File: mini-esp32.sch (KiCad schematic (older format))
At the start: 46 parts, among them J1 BAT, J2 USB_B_Micro, J5 Conn_01x18, J6 Conn_01x18, Q1 AO3401A, Q2 S8050, Q3 S8050, Q4 2N7002, SW1 RESET, U1 ESP32-WROOM-32D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

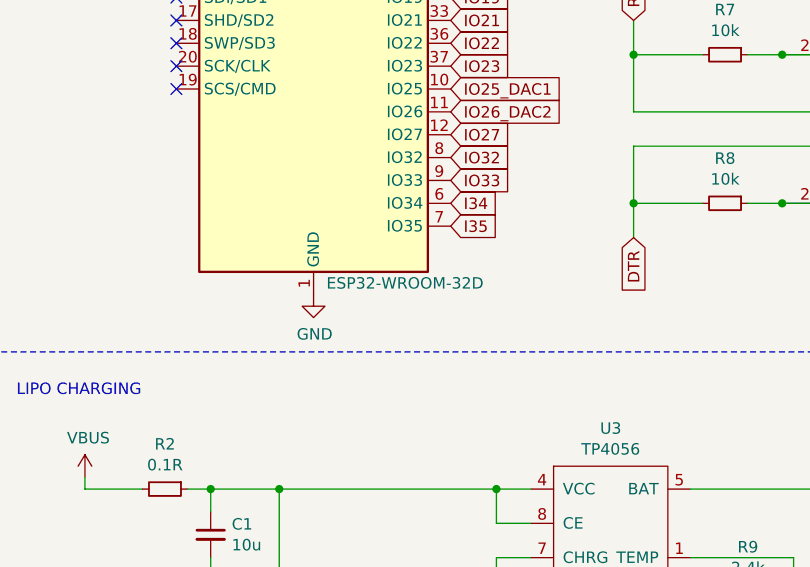
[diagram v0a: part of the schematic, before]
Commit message: Fix USB Micro B footprint to official one
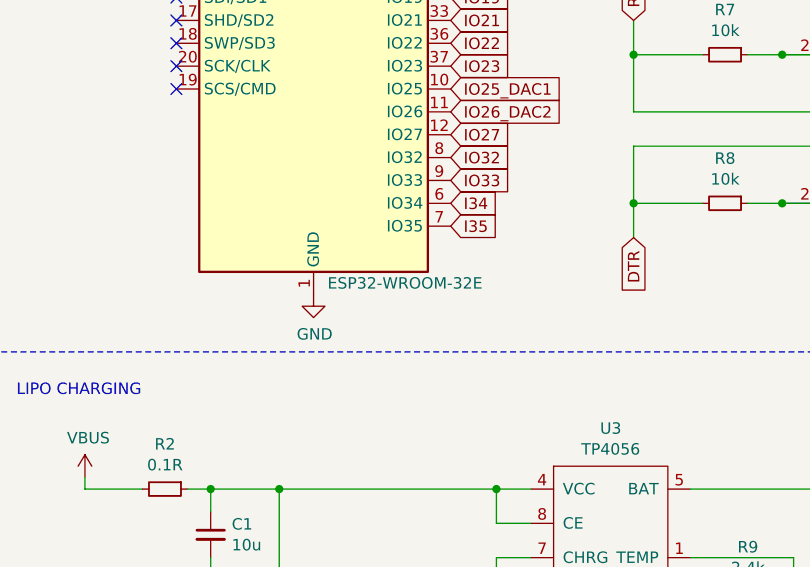
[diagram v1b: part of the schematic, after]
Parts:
- J2: footprint serialx:C10418 -> LCSC:USB_Micro-B_Jing-C10418-A01SB141B1-067
- U1: value ESP32-WROOM-32D -> ESP32-WROOM-32E; LCSC Part # (none) -> C701343
- U2: LCSC Part # (none) -> C841192
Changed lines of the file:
@@
 P 1950 4350
 F 0 "U1" H 2400 5700 50  0000 C CNN
-F 1 "ESP32-WROOM-32D" H 2350 3000 50  0000 C CNN
+F 1 "ESP32-WROOM-32E" H 2350 3000 50  0000 C CNN
 F 2 "RF_Module:ESP32-WROOM-32" H 1950 2850 50  0001 C CNN
 F 3 "https://www.espressif.com/sites/default/files/documentation/esp32-wroom-32d_esp32-wroom-32u_datasheet_en.pdf" H 1650 4400 50  0001 C CNN
+F 4 "C701343" H 1950 4350 50  0001 C CNN "LCSC Part #"
 	1    1950 4350
 	1    0    0    -1
@@
 F 2 "Package_TO_SOT_SMD:TSOT-23-5" H 3200 1150 50  0001 C CNN
 F 3 "" H 3200 1150 50  0001 C CNN
+F 4 "C841192" H 3200 1150 50  0001 C CNN "LCSC Part #"
 	1    3200 1150
 	1    0    0    -1
@@
 F 0 "J2" H 5657 4017 50  0000 C CNN
 F 1 "USB_B_Micro" H 5657 3926 50  0000 C CNN
-F 2 "serialx:C10418" H 5750 3500 50  0001 C CNN
+F 2 "LCSC:USB_Micro-B_Jing-C10418-A01SB141B1-067" H 5750 3500 50  0001 C CNN
 F 3 "~" H 5750 3500 50  0001 C CNN
 F 4 "C10418" H 5600 3550 50  0001 C CNN "LCSC Part #"

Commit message: Improved routing. Internal layers are not used anymore for routing.
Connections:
- net VBUS: no longer Q1.1 (G)
- net at D1.2 (A), FB1.1: now also Q1.1 (G)
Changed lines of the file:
@@
 $EndComp
-Wire Wire Line
-	1100 1000 1100 1100
 Wire Wire Line
 	1100 1500 1200 1500
@@
 	1100 1500 1100 1750
 Wire Wire Line
-	1500 1100 1100 1100
-Connection ~ 1100 1100
-Wire Wire Line
-	1100 1100 1100 1500
+	1500 1100 1450 1100
 $Comp
 L power:GND #PWR0114
@@
 NoConn ~ 10150 4150
 NoConn ~ 10150 4400
+Wire Wire Line
+	1450 1100 1450 1500
+Connection ~ 1450 1500
+Wire Wire Line
+	1100 1000 1100 1500
 $EndSCHEMATC

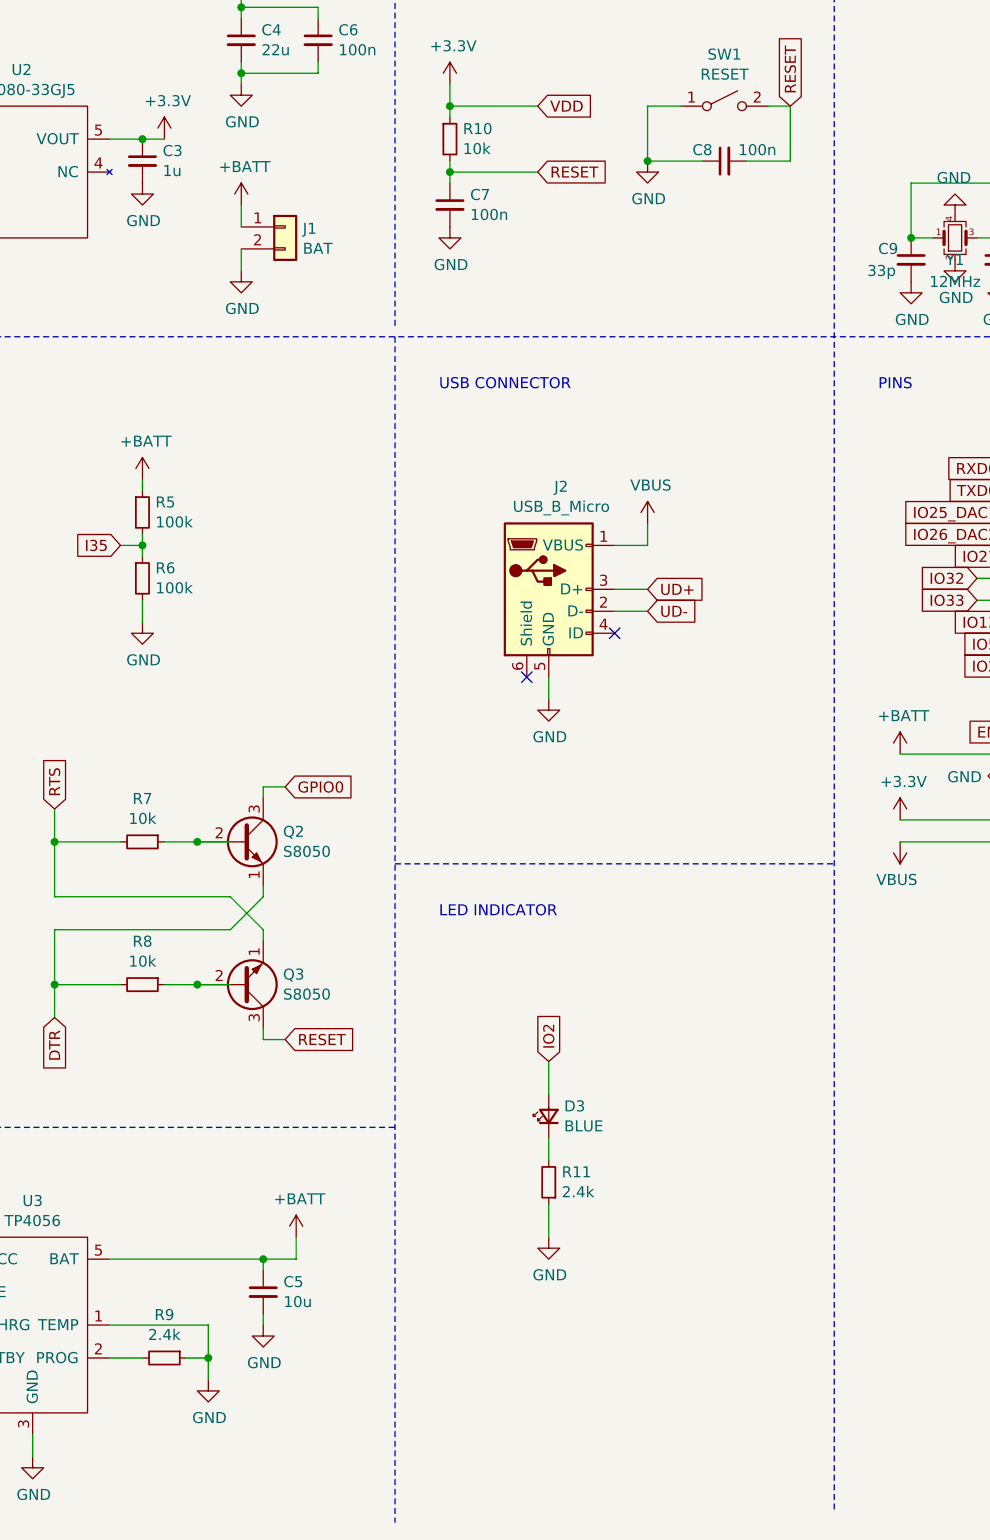
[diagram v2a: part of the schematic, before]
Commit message: Add FS312F-G battery protection IC
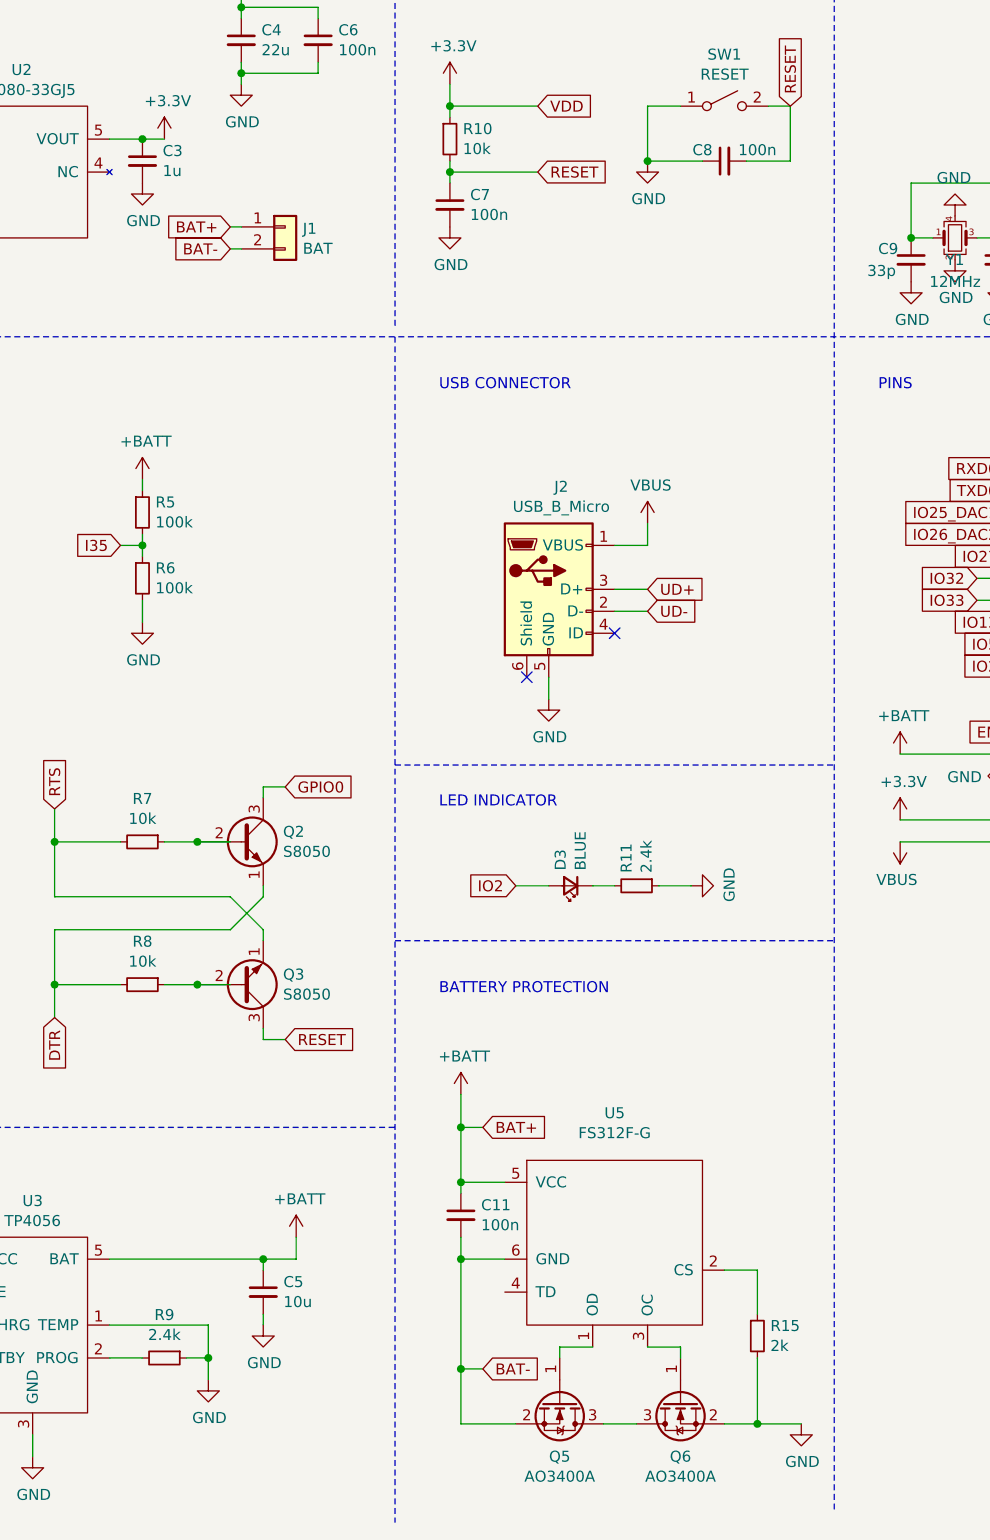
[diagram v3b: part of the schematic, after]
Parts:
- added C11: 100n, Capacitor_SMD:C_0402_1005Metric, symbol Device:C_Small
- added Q5, Q6: AO3400A, Package_TO_SOT_SMD:SOT-23, symbol Transistor_FET:AO3400A
- added R15: 2k, Resistor_SMD:R_0402_1005Metric, symbol Device:R_Small
- added U5: FS312F-G, Package_TO_SOT_SMD:SOT-23-6, symbol myLib:FS312F-G
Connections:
- net +BATT: now also C11.1, U5.5 (VCC)
- net GND: now also Q6.2 (S), R15.2; no longer J1.2 (Pin_2)
- new net: Q5.1 (G), U5.1 (OD)
- new net: R15.1, U5.2 (CS)
- new net: Q6.1 (G), U5.3 (OC)
- new net: Q5.3 (D), Q6.3 (D)
- new net BAT-: C11.2, J1.2 (Pin_2), Q5.2 (S), U5.6 (GND)
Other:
- note added: "BATTERY PROTECTION"
- moved on the sheet: D3, R11
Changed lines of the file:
@@
 $EndComp
-$Comp
-L power:GND #PWR0116
-U 1 1 5F8AD9AA
-P 4200 2100
-F 0 "#PWR0116" H 4200 1850 50  0001 C CNN
-F 1 "GND" H 4205 1927 50  0000 C CNN
-F 2 "" H 4200 2100 50  0001 C CNN
-F 3 "" H 4200 2100 50  0001 C CNN
-	1    4200 2100
-	1    0    0    -1
-$EndComp
-$Comp
-L power:+BATT #PWR0117
-U 1 1 5F8ADEC7
-P 4200 1800
-F 0 "#PWR0117" H 4200 1650 50  0001 C CNN
-F 1 "+BATT" H 4215 1973 50  0000 C CNN
-F 2 "" H 4200 1800 50  0001 C CNN
-F 3 "" H 4200 1800 50  0001 C CNN
-	1    4200 1800
-	1    0    0    -1
-$EndComp
-Wire Wire Line
-	4200 1900 4200 1800
-Wire Wire Line
-	4200 2000 4200 2100
 $Comp
 L power:GND #PWR0118
@@
 Wire Notes Line
 	4900 2400 4900 7800
-Text GLabel 5600 5700 1    50   Input ~ 0
-IO2
-$Comp
-L Device:LED_Small D3
-U 1 1 5FA28E7E
-P 5600 5950
-F 0 "D3" V 5646 5880 50  0000 R CNN
-F 1 "BLUE" V 5555 5880 50  0000 R CNN
-F 2 "LED_SMD:LED_0603_1608Metric" V 5600 5950 50  0001 C CNN
-F 3 "~" V 5600 5950 50  0001 C CNN
-F 4 "C72041" H 5600 5950 50  0001 C CNN "LCSC Part #"
-	1    5600 5950
-	0    -1   -1   0
-$EndComp
-$Comp
-L Device:R_Small R11
-U 1 1 5FA2B130
-P 5600 6250
-F 0 "R11" H 5541 6204 50  0000 R CNN
-F 1 "2.4k" H 5541 6295 50  0000 R CNN
-F 2 "Resistor_SMD:R_0603_1608Metric" H 5600 6250 50  0001 C CNN
-F 3 "~" H 5600 6250 50  0001 C CNN
-F 4 "C22940" H 5600 6250 50  0001 C CNN "LCSC Part #"
-	1    5600 6250
-	-1   0    0    1
-$EndComp
-$Comp
-L power:GND #PWR0131
-U 1 1 5FA2B7E3
-P 5600 6500
-F 0 "#PWR0131" H 5600 6250 50  0001 C CNN
-F 1 "GND" H 5605 6327 50  0000 C CNN
-F 2 "" H 5600 6500 50  0001 C CNN
-F 3 "" H 5600 6500 50  0001 C CNN
-	1    5600 6500
-	1    0    0    -1
-$EndComp
-Wire Wire Line
-	5600 5700 5600 5850
-Wire Wire Line
-	5600 6050 5600 6150
-Wire Wire Line
-	5600 6350 5600 6500
-Text Notes 5100 5050 0    50   ~ 0
+Text Notes 5100 4550 0    50   ~ 0
 LED INDICATOR
 Wire Notes Line
@@
 NoConn ~ 5500 3950
 Wire Notes Line
-	4900 4800 6900 4800
+	4900 4350 6900 4350
 Text Notes 5100 2650 0    50   ~ 0
 USB CONNECTOR
@@
 Wire Wire Line
 	1100 1000 1100 1500
+$Comp
+L power:+BATT #PWR0107
+U 1 1 5FBE7D4B
+P 5200 5850
+F 0 "#PWR0107" H 5200 5700 50  0001 C CNN
+F 1 "+BATT" H 5215 6023 50  0000 C CNN
+F 2 "" H 5200 5850 50  0001 C CNN
+F 3 "" H 5200 5850 50  0001 C CNN
+	1    5200 5850
+	1    0    0    -1
+$EndComp
+Wire Wire Line
+	5200 6600 5400 6600
+$Comp
+L Transistor_FET:AO3400A Q6
+U 1 1 5FBFA0D1
+P 6200 7250
+F 0 "Q6" V 6449 7250 50  0000 C CNN
+F 1 "AO3400A" V 6540 7250 50  0000 C CNN
+F 2 "Package_TO_SOT_SMD:SOT-23" H 6400 7175 50  0001 L CIN
+F 3 "http://www.aosmd.com/pdfs/datasheet/AO3400A.pdf" H 6200 7250 50  0001 L CNN
+	1    6200 7250
+	0    -1   1    0
+$EndComp
+Wire Wire Line
+	5850 7350 6000 7350
+$Comp
+L Transistor_FET:AO3400A Q5
+U 1 1 5FBF3F7C
+P 5650 7250
+F 0 "Q5" V 5899 7250 50  0000 C CNN
+F 1 "AO3400A" V 5990 7250 50  0000 C CNN
+F 2 "Package_TO_SOT_SMD:SOT-23" H 5850 7175 50  0001 L CIN
+F 3 "http://www.aosmd.com/pdfs/datasheet/AO3400A.pdf" H 5650 7250 50  0001 L CNN
+	1    5650 7250
+	0    1    1    0
+$EndComp
+Wire Wire Line
+	5650 7050 5650 7000
+Wire Wire Line
+	6200 7050 6200 7000
+Wire Wire Line
+	6750 7350 6550 7350
+$Comp
+L Device:R_Small R15
+U 1 1 5FC2A966
+P 6550 6950
+F 0 "R15" H 6609 6996 50  0000 L CNN
+F 1 "2k" H 6609 6905 50  0000 L CNN
+F 2 "Resistor_SMD:R_0402_1005Metric" H 6550 6950 50  0001 C CNN
+F 3 "~" H 6550 6950 50  0001 C CNN
+	1    6550 6950
+	1    0    0    -1
+$EndComp
+$Comp
+L myLib:FS312F-G U5
+U 1 1 5FBE4449
+P 5900 6000
+F 0 "U5" H 5900 6065 50  0000 C CNN
+F 1 "FS312F-G" H 5900 5974 50  0000 C CNN
+F 2 "Package_TO_SOT_SMD:SOT-23-6" H 5900 6000 50  0001 C CNN
+F 3 "" H 5900 6000 50  0001 C CNN
+	1    5900 6000
+	1    0    0    -1
+$EndComp
+Wire Wire Line
+	6550 7050 6550 7350
+Connection ~ 6550 7350
+Wire Wire Line
+	6550 7350 6400 7350
+Wire Wire Line
+	5200 7350 5200 7100
+$Comp
+L Device:C_Small C11
+U 1 1 5FC424C5
+P 5200 6400
+F 0 "C11" H 5292 6446 50  0000 L CNN
+F 1 "100n" H 5292 6355 50  0000 L CNN
+F 2 "Capacitor_SMD:C_0402_1005Metric" H 5200 6400 50  0001 C CNN
+F 3 "~" H 5200 6400 50  0001 C CNN
+	1    5200 6400
+	1    0    0    -1
+$EndComp
+Wire Wire Line
+	5200 6300 5200 6250
+Wire Wire Line
+	5200 6600 5200 6500
+Connection ~ 5200 6600
+Wire Wire Line
+	6100 4900 6250 4900
+Wire Wire Line
+	5800 4900 5900 4900
+Wire Wire Line
+	5450 4900 5600 4900
+$Comp
+L power:GND #PWR0131
+U 1 1 5FA2B7E3
+P 6250 4900
+F 0 "#PWR0131" H 6250 4650 50  0001 C CNN
+F 1 "GND" H 6255 4727 50  0000 C CNN
+F 2 "" H 6250 4900 50  0001 C CNN
+F 3 "" H 6250 4900 50  0001 C CNN
+	1    6250 4900
+	0    -1   -1   0
+$EndComp
+$Comp
+L Device:R_Small R11
+U 1 1 5FA2B130
+P 6000 4900
+F 0 "R11" H 5941 4854 50  0000 R CNN
+F 1 "2.4k" H 5941 4945 50  0000 R CNN
+F 2 "Resistor_SMD:R_0603_1608Metric" H 6000 4900 50  0001 C CNN
+F 3 "~" H 6000 4900 50  0001 C CNN
+F 4 "C22940" H 6000 4900 50  0001 C CNN "LCSC Part #"
+	1    6000 4900
+	0    1    1    0
+$EndComp
+Text GLabel 5450 4900 0    50   Input ~ 0
+IO2
+$Comp
+L Device:LED_Small D3
+U 1 1 5FA28E7E
+P 5700 4900
+F 0 "D3" V 5746 4830 50  0000 R CNN
+F 1 "BLUE" V 5655 4830 50  0000 R CNN
+F 2 "LED_SMD:LED_0603_1608Metric" V 5700 4900 50  0001 C CNN
+F 3 "~" V 5700 4900 50  0001 C CNN
+F 4 "C72041" H 5700 4900 50  0001 C CNN "LCSC Part #"
+	1    5700 4900
+	-1   0    0    1
+$EndComp
+Text GLabel 4150 1900 0    50   Input ~ 0
+BAT+
+Wire Wire Line
+	4150 2000 4200 2000
+Wire Wire Line
+	4150 1900 4200 1900
+Wire Wire Line
+	5400 6250 5200 6250
+Connection ~ 5200 6250
+Wire Wire Line
+	5200 6250 5200 6000
+Text GLabel 5300 6000 2    50   Input ~ 0
+BAT+
+Wire Wire Line
+	5300 6000 5200 6000
+Connection ~ 5200 6000
+Wire Wire Line
+	5200 6000 5200 5850
+Text GLabel 5300 7100 2    50   Input ~ 0
+BAT-
+Wire Wire Line
+	5300 7100 5200 7100
+Connection ~ 5200 7100
+Wire Wire Line
+	5200 7100 5200 6600
+$Comp
+L power:GND #PWR0108
+U 1 1 5FCB8A37
+P 6750 7350
+F 0 "#PWR0108" H 6750 7100 50  0001 C CNN
+F 1 "GND" H 6755 7177 50  0000 C CNN
+F 2 "" H 6750 7350 50  0001 C CNN
+F 3 "" H 6750 7350 50  0001 C CNN
+	1    6750 7350
+	1    0    0    -1
+$EndComp
+Text Notes 5100 5400 0    50   ~ 0
+BATTERY PROTECTION
+Wire Notes Line
+	4900 5150 6900 5150
+Wire Wire Line
+	5450 7350 5200 7350
+Wire Wire Line
+	5650 7000 5800 7000
+Wire Wire Line
+	6050 7000 6200 7000
+Wire Wire Line
+	6400 6650 6550 6650
+Wire Wire Line
+	6550 6650 6550 6850
+Text GLabel 4150 2000 0    50   Input ~ 0
+BAT-
 $EndSCHEMATC

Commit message: Polishing. V2.1.0
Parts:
- C11: LCSC Part # (none) -> C1525
- Q5, Q6: LCSC Part # (none) -> C20917
- R15: LCSC Part # (none) -> C4109
- U5: LCSC Part # (none) -> C82736
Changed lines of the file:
@@
 F 2 "Package_TO_SOT_SMD:SOT-23" H 6400 7175 50  0001 L CIN
 F 3 "http://www.aosmd.com/pdfs/datasheet/AO3400A.pdf" H 6200 7250 50  0001 L CNN
+F 4 "C20917" H 6200 7250 50  0001 C CNN "LCSC Part #"
 	1    6200 7250
 	0    -1   1    0
@@
 F 2 "Package_TO_SOT_SMD:SOT-23" H 5850 7175 50  0001 L CIN
 F 3 "http://www.aosmd.com/pdfs/datasheet/AO3400A.pdf" H 5650 7250 50  0001 L CNN
+F 4 "C20917" H 5650 7250 50  0001 C CNN "LCSC Part #"
 	1    5650 7250
 	0    1    1    0
@@
 F 2 "Resistor_SMD:R_0402_1005Metric" H 6550 6950 50  0001 C CNN
 F 3 "~" H 6550 6950 50  0001 C CNN
+F 4 "C4109" H 6550 6950 50  0001 C CNN "LCSC Part #"
 	1    6550 6950
 	1    0    0    -1
@@
 F 2 "Package_TO_SOT_SMD:SOT-23-6" H 5900 6000 50  0001 C CNN
 F 3 "" H 5900 6000 50  0001 C CNN
+F 4 "C82736" H 5900 6000 50  0001 C CNN "LCSC Part #"
 	1    5900 6000
 	1    0    0    -1
@@
 F 2 "Capacitor_SMD:C_0402_1005Metric" H 5200 6400 50  0001 C CNN
 F 3 "~" H 5200 6400 50  0001 C CNN
+F 4 "C1525" H 5200 6400 50  0001 C CNN "LCSC Part #"
 	1    5200 6400
 	1    0    0    -1
